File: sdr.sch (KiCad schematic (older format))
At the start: 9 parts

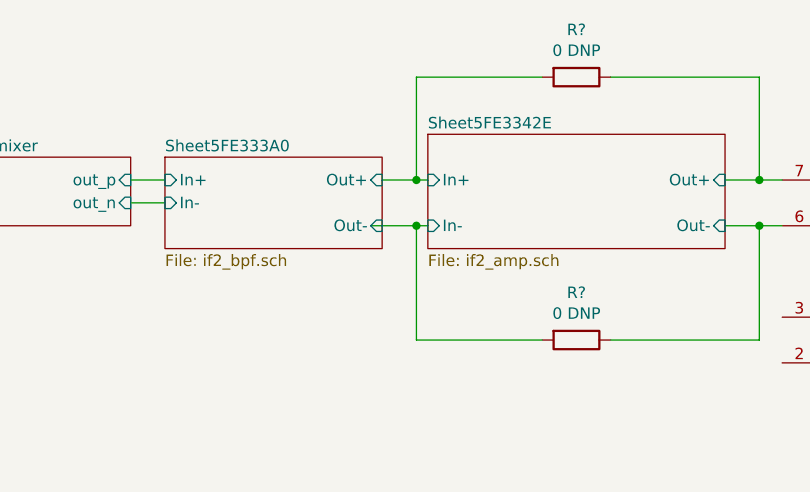
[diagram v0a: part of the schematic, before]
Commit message: If2 50 ohm filter
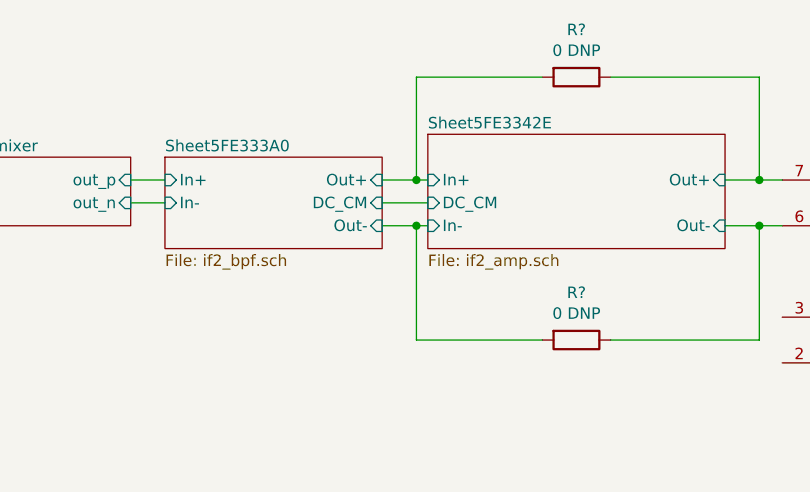
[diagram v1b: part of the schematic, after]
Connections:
- wire segments 41 -> 42
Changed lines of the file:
@@
 F4 "In+" I L 6700 1300 50
 F5 "In-" I L 6700 1400 50
+F6 "DC_CM" I R 7650 1400 50
 $EndSheet
 $Sheet
@@
 F4 "Out+" I R 9150 1300 50
 F5 "Out-" I R 9150 1500 50
+F6 "DC_CM" I L 7850 1400 50
 $EndSheet
 $Comp
@@
 Connection ~ 7800 1300
 Wire Wire Line
-	7600 1500 7800 1500
+	7800 1500 7850 1500
+Wire Wire Line
+	6700 1300 6550 1300
+Wire Wire Line
+	6550 1400 6700 1400
+Wire Wire Line
+	7650 1500 7800 1500
 Connection ~ 7800 1500
 Wire Wire Line
-	7800 1500 7850 1500
-Wire Wire Line
-	6700 1300 6550 1300
-Wire Wire Line
-	6550 1400 6700 1400
+	7650 1400 7850 1400
 $EndSCHEMATC

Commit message: Tx initial commit
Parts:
- added U?: AD9744, Package_SO:TSSOP-28_4.4x9.7mm_P0.65mm, symbol Analog_DAC:AD9744
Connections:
- net at U?.6 (LO): now also K?.9; no longer K?.7
- net at K?.4: now also K?.7; no longer K?.9
- net Tx filter/OUT: now reaches K?.8
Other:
- note added: "+19 dBm"
- note added: "PA?"
- note removed: "Switchable bga2866??"
- moved on the sheet: K?C
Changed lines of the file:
@@
 $Descr A4 11693 8268
 encoding utf-8
-Sheet 1 7
+Sheet 1 9
 Title ""
 Date ""
@@
 L Relay:FRT5_separated K?
 U 3 1 5FE89BA9
-P 2200 4100
-F 0 "K?" H 2344 4146 50  0000 L CNN
-F 1 "FRT5_separated" H 2344 4055 50  0000 L CNN
-F 2 "Relay_THT:Relay_DPDT_FRT5" H 2400 4000 50  0001 L CNN
-F 3 "https://www.elpro.org/de/index.php?controller=attachment&id_attachment=8663" H 2200 4100 50  0001 C CNN
-	3    2200 4100
-	1    0    0    -1
+P 6200 4250
+F 0 "K?" H 6344 4296 50  0000 L CNN
+F 1 "FRT5_separated" H 6344 4205 50  0000 L CNN
+F 2 "Relay_THT:Relay_DPDT_FRT5" H 6400 4150 50  0001 L CNN
+F 3 "https://www.elpro.org/de/index.php?controller=attachment&id_attachment=8663" H 6200 4250 50  0001 C CNN
+	3    6200 4250
+	0    -1   1    0
 $EndComp
 Wire Wire Line
@@
 	1200 3650 1050 3650
 Wire Wire Line
-	2100 3800 2100 3750
-Wire Wire Line
 	2100 3750 1800 3750
 Wire Wire Line
-	2300 3800 2300 2100
-Wire Wire Line
-	2300 2100 3300 2100
-Wire Wire Line
 	3300 2100 3300 1750
-Wire Wire Line
-	2200 4400 10750 4400
-Wire Wire Line
-	10750 4400 10750 5100
-Text Notes 4650 1800 0    50   ~ 0
-Switchable bga2866??
 $Comp
 L Device:R R?
@@
 Wire Wire Line
 	7650 1400 7850 1400
+$Comp
+L Analog_DAC:AD9744 U?
+U 1 1 5FF3A0F3
+P 10150 4700
+F 0 "U?" H 10150 5881 50  0000 C CNN
+F 1 "AD9744" H 10150 5790 50  0000 C CNN
+F 2 "Package_SO:TSSOP-28_4.4x9.7mm_P0.65mm" H 10750 4900 50  0001 C CNN
+F 3 "https://www.analog.com/media/en/technical-documentation/data-sheets/AD9744.pdf" H 10750 4900 50  0001 C CNN
+	1    10150 4700
+	-1   0    0    -1
+$EndComp
+$Sheet
+S 7500 4100 1000 300
+U 5FF487A7
+F0 "Tx Preamp" 50
+F1 "tx_preamp.sch" 50
+F2 "IN_P" I R 8500 4200 50
+F3 "IN_N" I R 8500 4300 50
+F4 "OUT" I L 7500 4250 50
+$EndSheet
+$Sheet
+S 6500 4100 850  300
+U 5FF5AE54
+F0 "Tx filter" 50
+F1 "tx_filter.sch" 50
+F2 "IN" I R 7350 4250 50
+F3 "OUT" I L 6500 4250 50
+$EndSheet
+Wire Wire Line
+	7350 4250 7500 4250
+Wire Wire Line
+	5900 4150 5500 4150
+Wire Wire Line
+	5500 4150 5500 2100
+Wire Wire Line
+	5500 2100 3300 2100
+Wire Wire Line
+	5900 4350 2100 4350
+Wire Wire Line
+	2100 3750 2100 4350
+Text Notes 3250 4450 0    50   ~ 0
+PA?
+Text Notes 6000 4050 0    50   ~ 0
++19 dBm
 $EndSCHEMATC

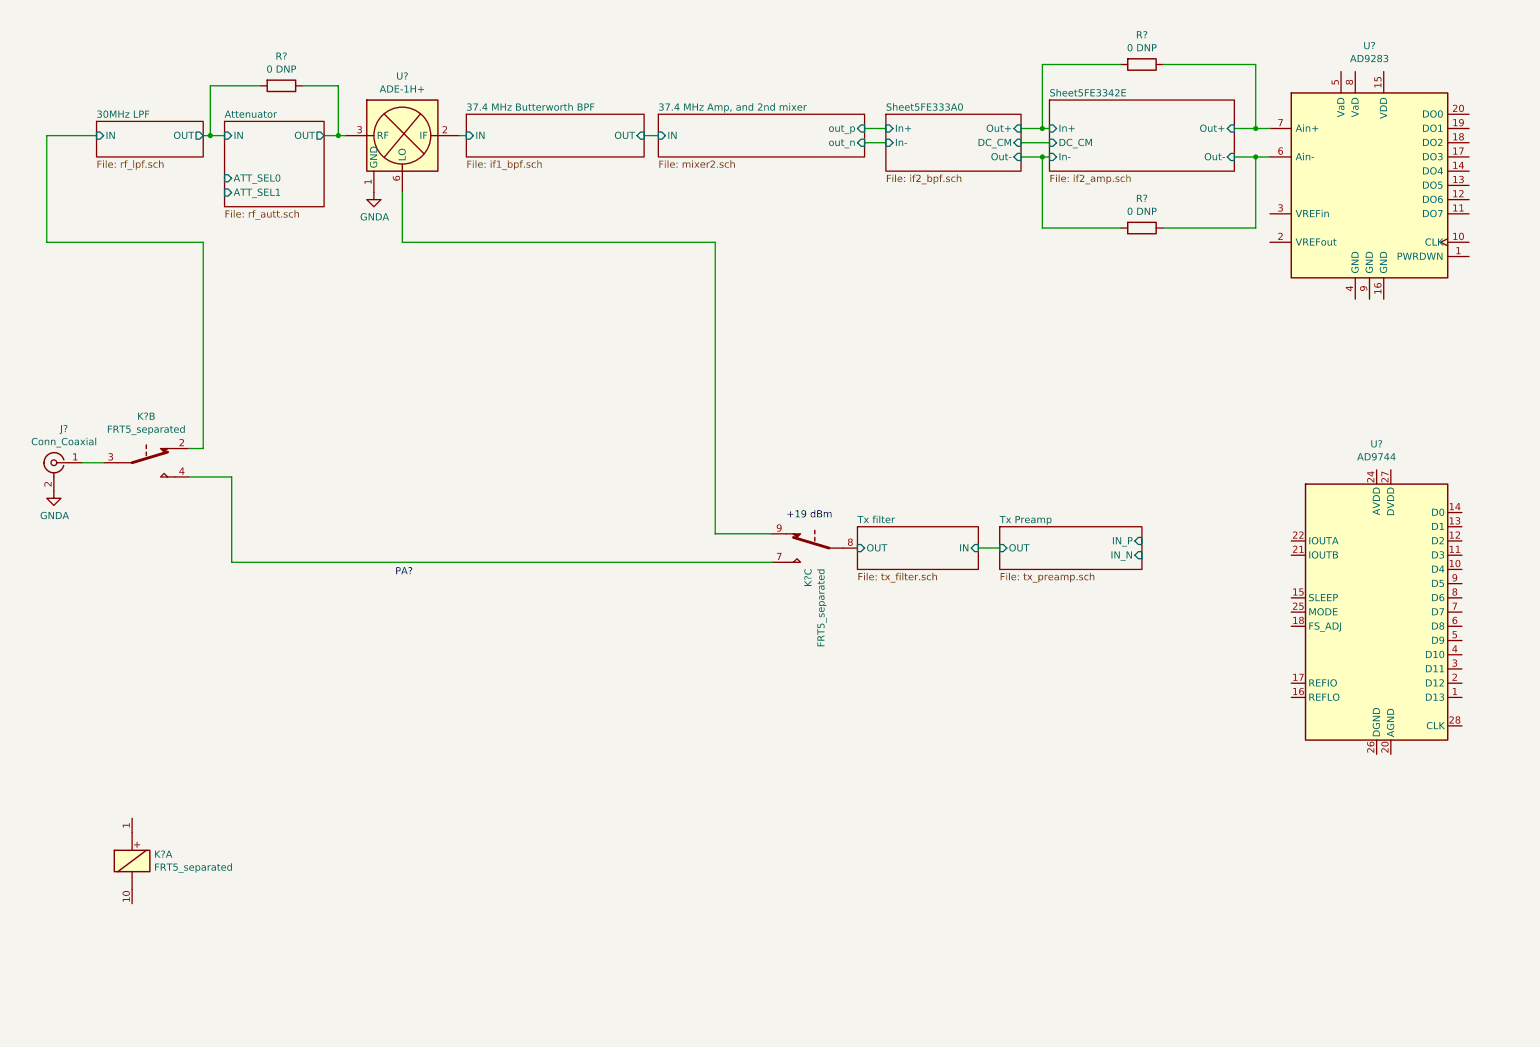
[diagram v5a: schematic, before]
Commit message: SDR-FPGA Interface v0
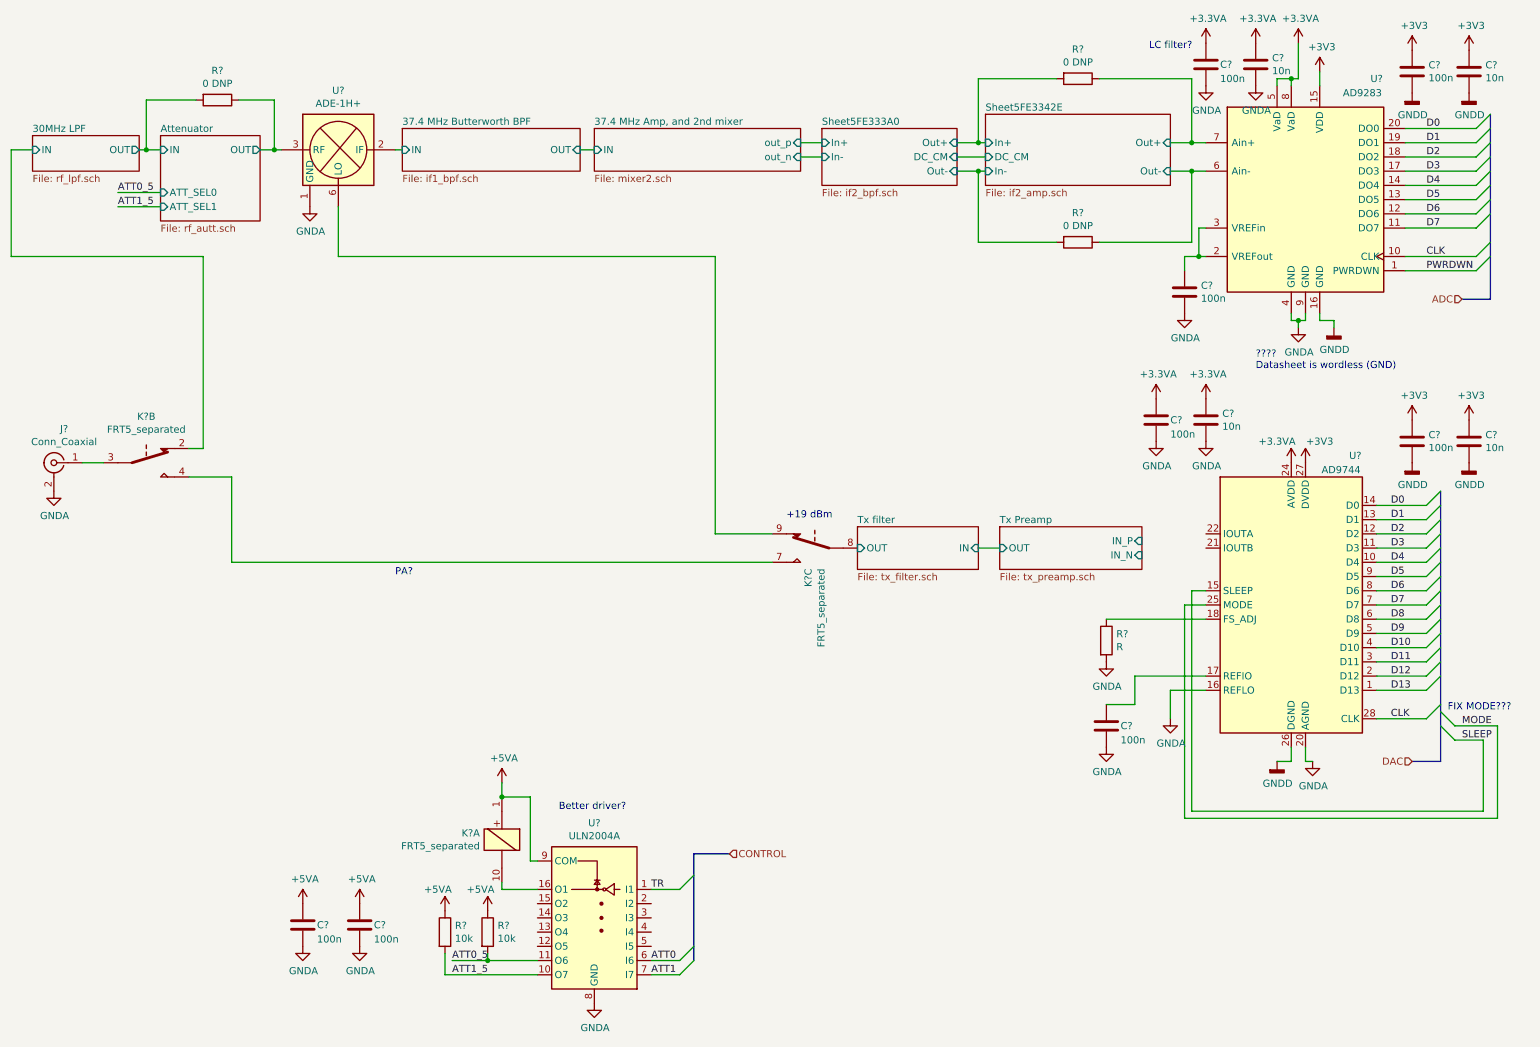
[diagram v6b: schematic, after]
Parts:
- added C? (x8): 100n, symbol Device:C
- added C? (x4): 10n, symbol Device:C
- added R?: R, symbol Device:R
- added R? (x2): 10k, symbol Device:R
- added U?: ULN2004A, symbol Transistor_Array:ULN2004A
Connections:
- net GNDA: now also U?.16 (REFLO), U?.20 (AGND), U?.4 (GND), U?.9 (GND), C?.2, C?.2, C?.2, C?.2, C?.2, C?.2, C?.2, C?.2, R?.2, U?.8 (GND)
- net PWRDWN: now reaches U?.1 (PWRDWN)
- net CLK: now reaches U?.10 (CLK)
- net CLK: now also U?.28 (CLK)
- net D7: now reaches U?.11 (DO7)
- net D7: now also U?.7 (D7)
- net D6: now reaches U?.12 (DO6)
- net D6: now also U?.8 (D6)
- net D5: now reaches U?.13 (DO5)
- net D5: now also U?.9 (D5)
- net D4: now reaches U?.14 (DO4)
- net D4: now also U?.10 (D4)
- net +3V3: now reaches U?.15 (VDD)
- net +3V3: now also U?.27 (DVDD), C?.1, C?.1, C?.1, C?.1
- net GNDD: now reaches U?.16 (GND)
- net GNDD: now also U?.26 (DGND), C?.2, C?.2, C?.2, C?.2
- net D3: now reaches U?.17 (DO3)
- net D3: now also U?.11 (D3)
- net D2: now reaches U?.18 (DO2)
- net D2: now also U?.12 (D2)
- net D1: now reaches U?.19 (DO1)
- net D1: now also U?.13 (D1)
- net at U?.2 (VREFout): now also U?.3 (VREFin), C?.1
- net D0: now reaches U?.20 (DO0)
- net D0: now also U?.14 (D0)
- net +3.3VA: now reaches U?.5 (VaD)
- net +3.3VA: now also U?.24 (AVDD), U?.8 (VaD), C?.1, C?.1, C?.1, C?.1
- net +5VA: now reaches K?.1
- net +5VA: now also C?.1, C?.1, R?.1, R?.1, U?.9 (COM)
- net at K?.10: now also U?.16 (O1)
- net D13: now reaches U?.1 (D13)
- net SLEEP: now reaches U?.15 (SLEEP)
- net at U?.17 (REFIO): now also C?.1
- net at U?.18 (FS_ADJ): now also R?.1
- net D12: now reaches U?.2 (D12)
- net MODE: now reaches U?.25 (MODE)
- net D11: now reaches U?.3 (D11)
- net D10: now reaches U?.4 (D10)
- net D9: now reaches U?.5 (D9)
- net D8: now reaches U?.6 (D8)
- new net ATT0: U?.6 (I6)
- new net ATT0_5: R?.2, U?.11 (O6)
- new net ATT1: U?.7 (I7)
- new net ATT1_5: R?.2, U?.10 (O7)
- new net TR: U?.1 (I1)
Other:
- note added: "????\nDatasheet is wordless (GND)"
- note added: "Better driver?"
- note added: "FIX MODE???"
- note added: "LC filter?"
- moved on the sheet: K?A, R?, U?

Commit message: Add notes to sdr.sch
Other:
- note added: "Undriven wires may collect noise?"
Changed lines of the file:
@@
 Wire Bus Line
 	10600 3850 10600 5750
+Text Notes 3000 7400 0    50   ~ 0
+Undriven wires may collect noise?
 $EndSCHEMATC
